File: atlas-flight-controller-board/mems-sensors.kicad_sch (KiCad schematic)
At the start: 11 parts

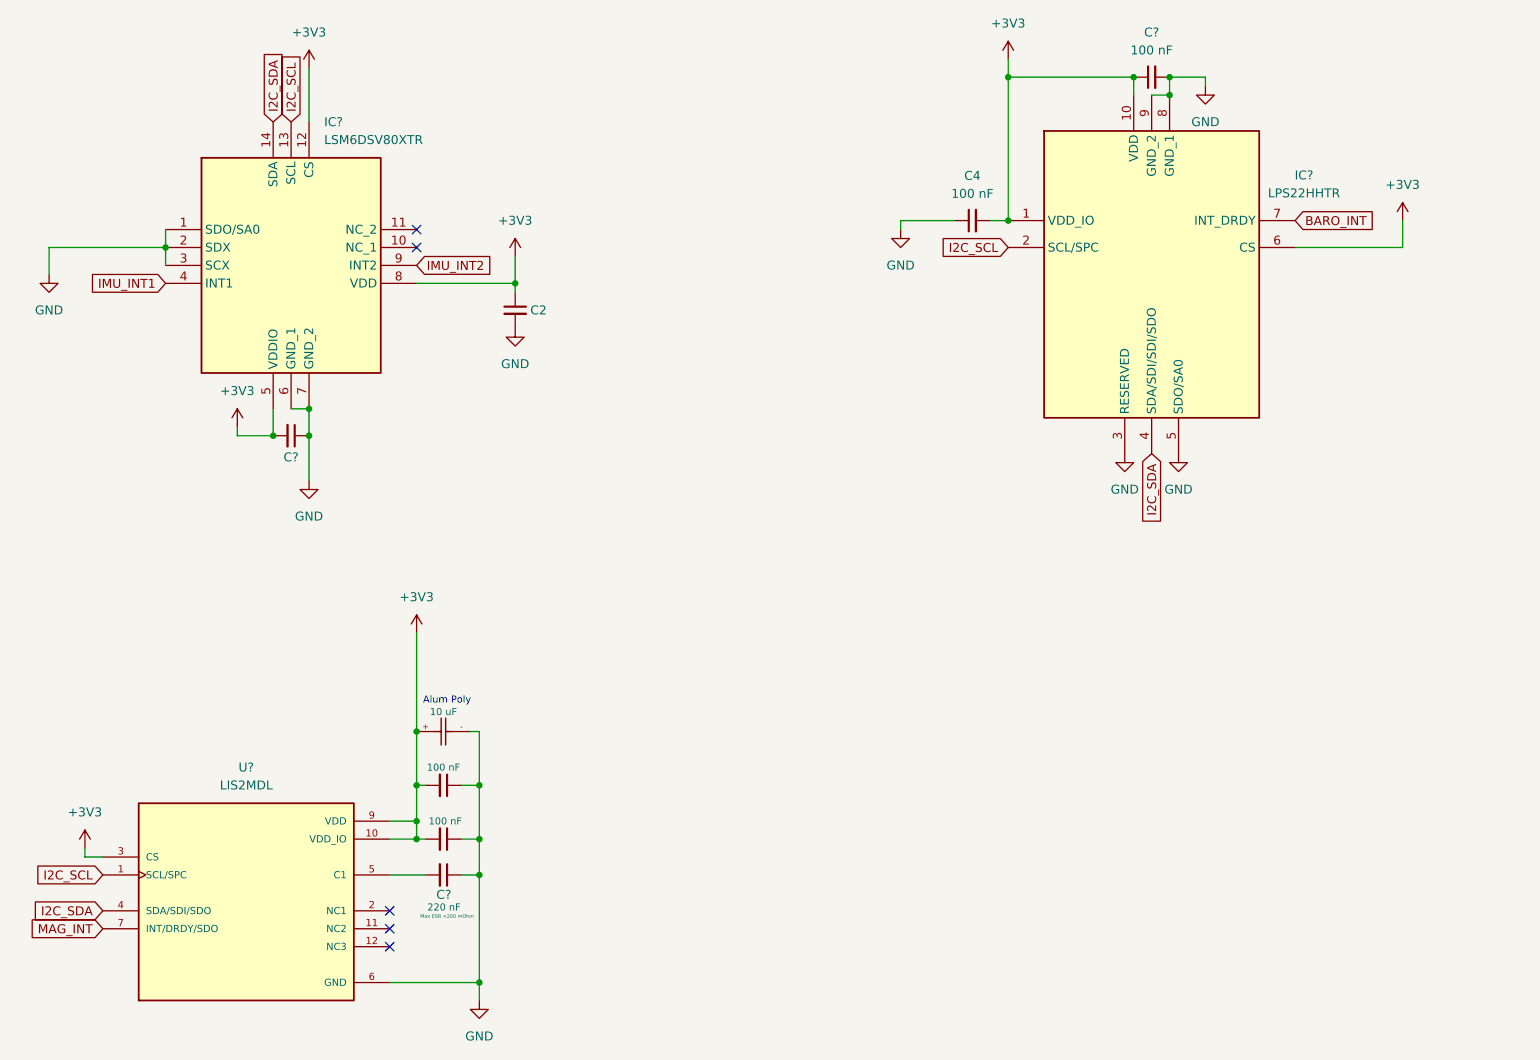
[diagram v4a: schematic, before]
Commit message: Added Regulator, Leaving disconnected, and off pcb for now as teensy board does this automatically. Leaving on for future revs without teensy board
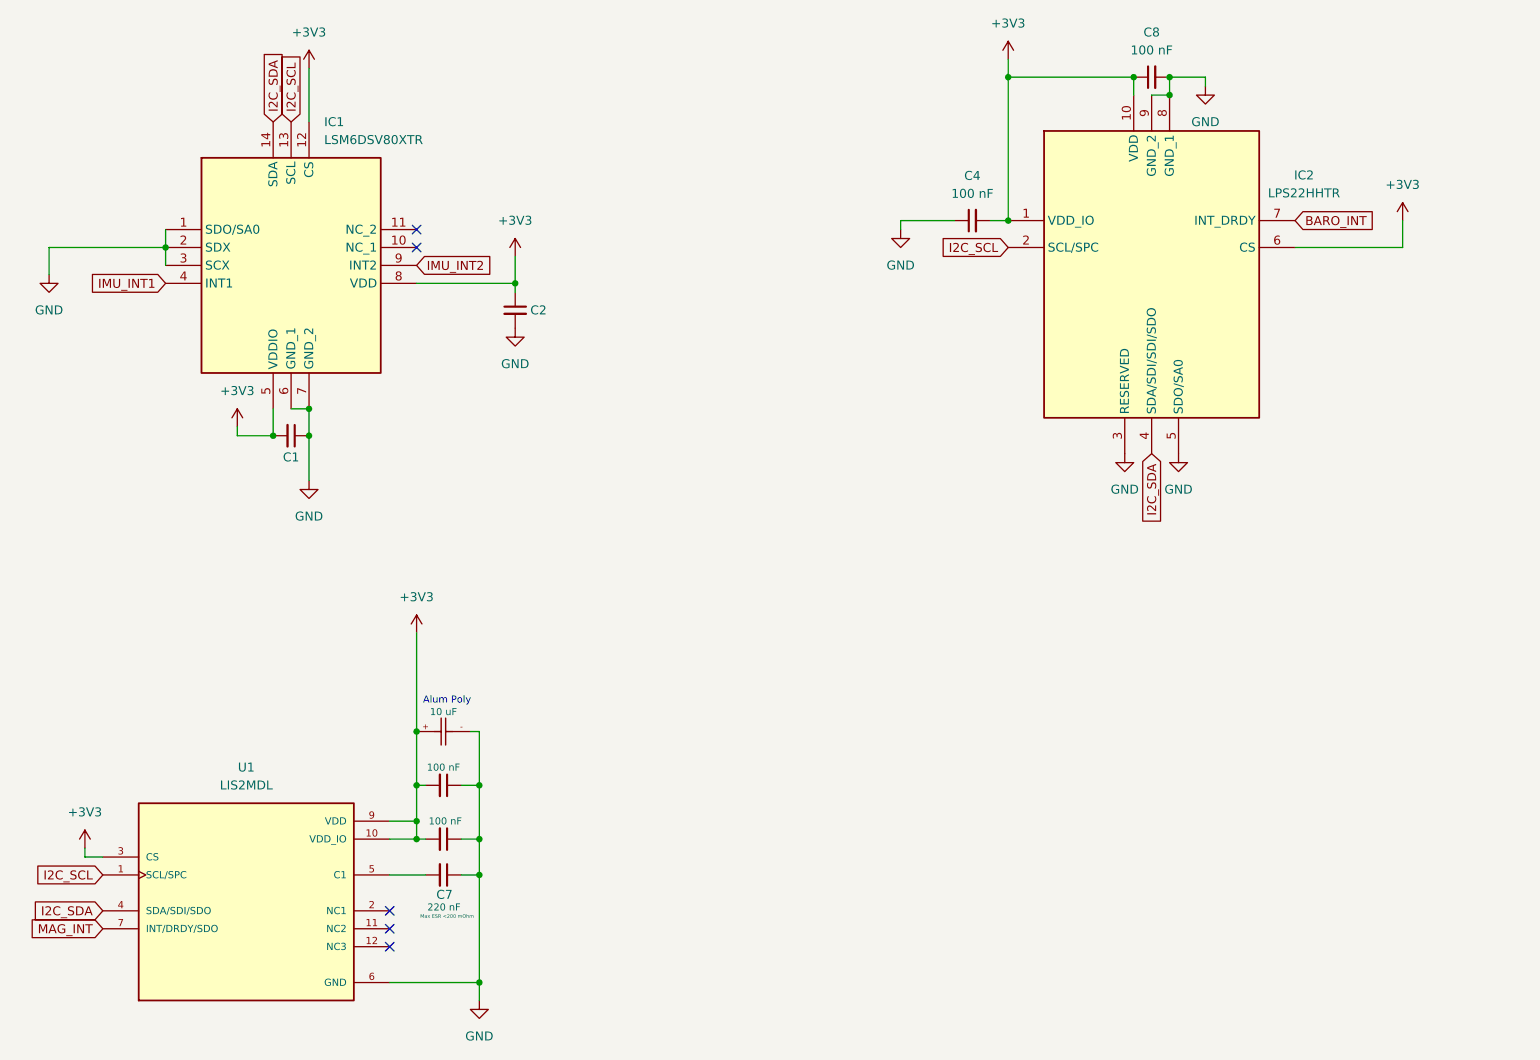
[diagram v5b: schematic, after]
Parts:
- gave numbers to parts that had none: 9
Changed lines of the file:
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@@
 		(on_board yes)
 		(dnp no)
-		(property "Reference" "C?"
+		(property "Reference" "C5"
 			(at 102.8636 134.62 90)
 			(effects
@@
 			(project "atlas-flight-controller-board"
 				(path "/99efb2d6-b5f7-438c-9ed2-f359400f01a1/5584e1ef-6e93-420a-9bdf-15a5926ce2b3"
-					(reference "C?")
+					(reference "C5")
 					(unit 1)
 				)
@@
 		(dnp no)
 		(fields_autoplaced yes)
-		(property "Reference" "#PWR?"
+		(property "Reference" "#PWR0109"
 			(at 46.99 74.93 0)
 			(effects
@@
 			(project "atlas-flight-controller-board"
 				(path "/99efb2d6-b5f7-438c-9ed2-f359400f01a1/5584e1ef-6e93-420a-9bdf-15a5926ce2b3"
-					(reference "#PWR?")
+					(reference "#PWR0109")
 					(unit 1)
 				)
@@
 		(dnp no)
 		(fields_autoplaced yes)
-		(property "Reference" "#PWR?"
+		(property "Reference" "#PWR0108"
 			(at 99.06 123.19 0)
 			(effects
@@
 			(project "atlas-flight-controller-board"
 				(path "/99efb2d6-b5f7-438c-9ed2-f359400f01a1/5584e1ef-6e93-420a-9bdf-15a5926ce2b3"
-					(reference "#PWR?")
+					(reference "#PWR0108")
 					(unit 1)
 				)
@@
 		(dnp no)
 		(fields_autoplaced yes)
-		(property "Reference" "#PWR?"
+		(property "Reference" "#PWR0113"
 			(at 113.03 69.85 0)
 			(effects
@@
 			(project "atlas-flight-controller-board"
 				(path "/99efb2d6-b5f7-438c-9ed2-f359400f01a1/5584e1ef-6e93-420a-9bdf-15a5926ce2b3"
-					(reference "#PWR?")
+					(reference "#PWR0113")
 					(unit 1)
 				)
@@
 		(dnp no)
 		(fields_autoplaced yes)
-		(property "Reference" "#PWR?"
+		(property "Reference" "#PWR0112"
 			(at 83.82 104.14 0)
 			(effects
@@
 			(project "atlas-flight-controller-board"
 				(path "/99efb2d6-b5f7-438c-9ed2-f359400f01a1/5584e1ef-6e93-420a-9bdf-15a5926ce2b3"
-					(reference "#PWR?")
+					(reference "#PWR0112")
 					(unit 1)
 				)
@@
 		(dnp no)
 		(fields_autoplaced yes)
-		(property "Reference" "#PWR?"
+		(property "Reference" "#PWR0103"
 			(at 210.82 48.26 0)
 			(effects
@@
 			(project "atlas-flight-controller-board"
 				(path "/99efb2d6-b5f7-438c-9ed2-f359400f01a1/5584e1ef-6e93-420a-9bdf-15a5926ce2b3"
-					(reference "#PWR?")
+					(reference "#PWR0103")
 					(unit 1)
 				)
@@
 		(dnp no)
 		(fields_autoplaced yes)
-		(property "Reference" "#PWR?"
+		(property "Reference" "#PWR0105"
 			(at 182.88 41.91 0)
 			(effects
@@
 			(project "atlas-flight-controller-board"
 				(path "/99efb2d6-b5f7-438c-9ed2-f359400f01a1/5584e1ef-6e93-420a-9bdf-15a5926ce2b3"
-					(reference "#PWR?")
+					(reference "#PWR0105")
 					(unit 1)
 				)
@@
 		(on_board yes)
 		(dnp no)
-		(property "Reference" "C?"
+		(property "Reference" "C6"
 			(at 102.616 144.272 90)
 			(effects
@@
 			(project "atlas-flight-controller-board"
 				(path "/99efb2d6-b5f7-438c-9ed2-f359400f01a1/5584e1ef-6e93-420a-9bdf-15a5926ce2b3"
-					(reference "C?")
+					(reference "C6")
 					(unit 1)
 				)
@@
 		(dnp no)
 		(fields_autoplaced yes)
-		(property "Reference" "IC?"
+		(property "Reference" "IC2"
 			(at 224.79 54.5398 0)
 			(effects
@@
 			(project "atlas-flight-controller-board"
 				(path "/99efb2d6-b5f7-438c-9ed2-f359400f01a1/5584e1ef-6e93-420a-9bdf-15a5926ce2b3"
-					(reference "IC?")
+					(reference "IC2")
 					(unit 1)
 				)
@@
 		(on_board yes)
 		(dnp no)
-		(property "Reference" "C?"
+		(property "Reference" "C3"
 			(at 102.87 127 0)
 			(effects
@@
 			(project "atlas-flight-controller-board"
 				(path "/99efb2d6-b5f7-438c-9ed2-f359400f01a1/5584e1ef-6e93-420a-9bdf-15a5926ce2b3"
-					(reference "C?")
+					(reference "C3")
 					(unit 1)
 				)
@@
 		(dnp no)
 		(fields_autoplaced yes)
-		(property "Reference" "C?"
+		(property "Reference" "C8"
 			(at 203.2063 34.29 90)
 			(effects
@@
 			(project "atlas-flight-controller-board"
 				(path "/99efb2d6-b5f7-438c-9ed2-f359400f01a1/5584e1ef-6e93-420a-9bdf-15a5926ce2b3"
-					(reference "C?")
+					(reference "C8")
 					(unit 1)
 				)
@@
 		(dnp no)
 		(fields_autoplaced yes)
-		(property "Reference" "#PWR?"
+		(property "Reference" "#PWR0110"
 			(at 73.66 93.98 0)
 			(effects
@@
 			(project "atlas-flight-controller-board"
 				(path "/99efb2d6-b5f7-438c-9ed2-f359400f01a1/5584e1ef-6e93-420a-9bdf-15a5926ce2b3"
-					(reference "#PWR?")
+					(reference "#PWR0110")
 					(unit 1)
 				)
@@
 		(dnp no)
 		(fields_autoplaced yes)
-		(property "Reference" "#PWR?"
+		(property "Reference" "#PWR0102"
 			(at 167.64 68.58 0)
 			(effects
@@
 			(project "atlas-flight-controller-board"
 				(path "/99efb2d6-b5f7-438c-9ed2-f359400f01a1/5584e1ef-6e93-420a-9bdf-15a5926ce2b3"
-					(reference "#PWR?")
+					(reference "#PWR0102")
 					(unit 1)
 				)
@@
 		(on_board yes)
 		(dnp no)
-		(property "Reference" "C?"
+		(property "Reference" "C1"
 			(at 81.28 94.488 90)
 			(effects
@@
 			(project "atlas-flight-controller-board"
 				(path "/99efb2d6-b5f7-438c-9ed2-f359400f01a1/5584e1ef-6e93-420a-9bdf-15a5926ce2b3"
-					(reference "C?")
+					(reference "C1")
 					(unit 1)
 				)
@@
 		(dnp no)
 		(fields_autoplaced yes)
-		(property "Reference" "#PWR?"
+		(property "Reference" "#PWR0101"
 			(at 107.95 177.8 0)
 			(effects
@@
 			(project "atlas-flight-controller-board"
 				(path "/99efb2d6-b5f7-438c-9ed2-f359400f01a1/5584e1ef-6e93-420a-9bdf-15a5926ce2b3"
-					(reference "#PWR?")
+					(reference "#PWR0101")
 					(unit 1)
 				)
@@
 		(dnp no)
 		(fields_autoplaced yes)
-		(property "Reference" "U?"
+		(property "Reference" "U1"
 			(at 74.93 138.43 0)
 			(effects
@@
 			(project "atlas-flight-controller-board"
 				(path "/99efb2d6-b5f7-438c-9ed2-f359400f01a1/5584e1ef-6e93-420a-9bdf-15a5926ce2b3"
-					(reference "U?")
+					(reference "U1")
 					(unit 1)
 				)
@@
 		(dnp no)
 		(fields_autoplaced yes)
-		(property "Reference" "#PWR?"
+		(property "Reference" "#PWR0111"
 			(at 52.07 153.67 0)
 			(effects
@@
 			(project "atlas-flight-controller-board"
 				(path "/99efb2d6-b5f7-438c-9ed2-f359400f01a1/5584e1ef-6e93-420a-9bdf-15a5926ce2b3"
-					(reference "#PWR?")
+					(reference "#PWR0111")
 					(unit 1)
 				)
@@
 		(dnp no)
 		(fields_autoplaced yes)
-		(property "Reference" "#PWR?"
+		(property "Reference" "#PWR0114"
 			(at 83.82 43.18 0)
 			(effects
@@
 			(project "atlas-flight-controller-board"
 				(path "/99efb2d6-b5f7-438c-9ed2-f359400f01a1/5584e1ef-6e93-420a-9bdf-15a5926ce2b3"
-					(reference "#PWR?")
+					(reference "#PWR0114")
 					(unit 1)
 				)
@@
 		(dnp no)
 		(fields_autoplaced yes)
-		(property "Reference" "#PWR?"
+		(property "Reference" "#PWR0106"
 			(at 207.01 100.33 0)
 			(effects
@@
 			(project "atlas-flight-controller-board"
 				(path "/99efb2d6-b5f7-438c-9ed2-f359400f01a1/5584e1ef-6e93-420a-9bdf-15a5926ce2b3"
-					(reference "#PWR?")
+					(reference "#PWR0106")
 					(unit 1)
 				)
@@
 		(on_board yes)
 		(dnp no)
-		(property "Reference" "C?"
+		(property "Reference" "C7"
 			(at 101.854 156.464 90)
 			(effects
@@
 			(project "atlas-flight-controller-board"
 				(path "/99efb2d6-b5f7-438c-9ed2-f359400f01a1/5584e1ef-6e93-420a-9bdf-15a5926ce2b3"
-					(reference "C?")
+					(reference "C7")
 					(unit 1)
 				)
@@
 		(dnp no)
 		(fields_autoplaced yes)
-		(property "Reference" "#PWR?"
+		(property "Reference" "#PWR0104"
 			(at 238.76 64.77 0)
 			(effects
@@
 			(project "atlas-flight-controller-board"
 				(path "/99efb2d6-b5f7-438c-9ed2-f359400f01a1/5584e1ef-6e93-420a-9bdf-15a5926ce2b3"
-					(reference "#PWR?")
+					(reference "#PWR0104")
 					(unit 1)
 				)
@@
 		(dnp no)
 		(fields_autoplaced yes)
-		(property "Reference" "#PWR?"
+		(property "Reference" "#PWR0107"
 			(at 199.39 100.33 0)
 			(effects
@@
 			(project "atlas-flight-controller-board"
 				(path "/99efb2d6-b5f7-438c-9ed2-f359400f01a1/5584e1ef-6e93-420a-9bdf-15a5926ce2b3"
-					(reference "#PWR?")
+					(reference "#PWR0107")
 					(unit 1)
 				)
@@
 		(dnp no)
 		(fields_autoplaced yes)
-		(property "Reference" "IC?"
+		(property "Reference" "IC1"
 			(at 85.9633 46.99 0)
 			(effects
@@
 			(project "atlas-flight-controller-board"
 				(path "/99efb2d6-b5f7-438c-9ed2-f359400f01a1/5584e1ef-6e93-420a-9bdf-15a5926ce2b3"
-					(reference "IC?")
+					(reference "IC1")
 					(unit 1)
 				)
@@
 		(dnp no)
 		(fields_autoplaced yes)
-		(property "Reference" "#PWR?"
+		(property "Reference" "#PWR0115"
 			(at 113.03 82.55 0)
 			(effects
@@
 			(project "atlas-flight-controller-board"
 				(path "/99efb2d6-b5f7-438c-9ed2-f359400f01a1/5584e1ef-6e93-420a-9bdf-15a5926ce2b3"
-					(reference "#PWR?")
-					(unit 1)
-				)
+					(reference "#PWR0115")
+					(unit 1)
+				)

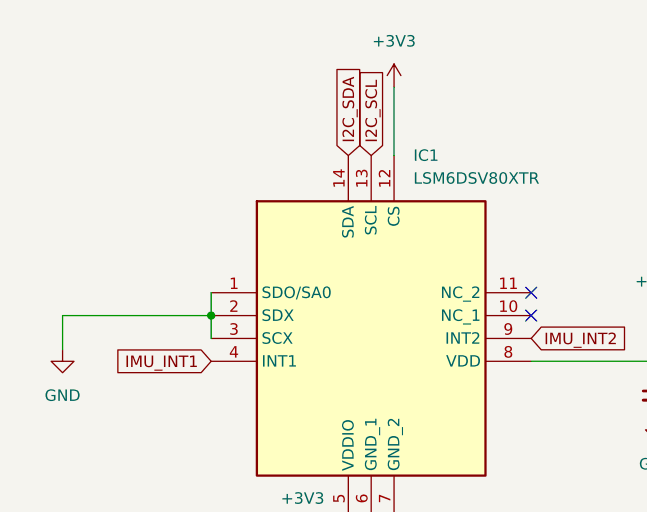
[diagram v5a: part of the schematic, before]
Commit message: Updating IMU to SPI
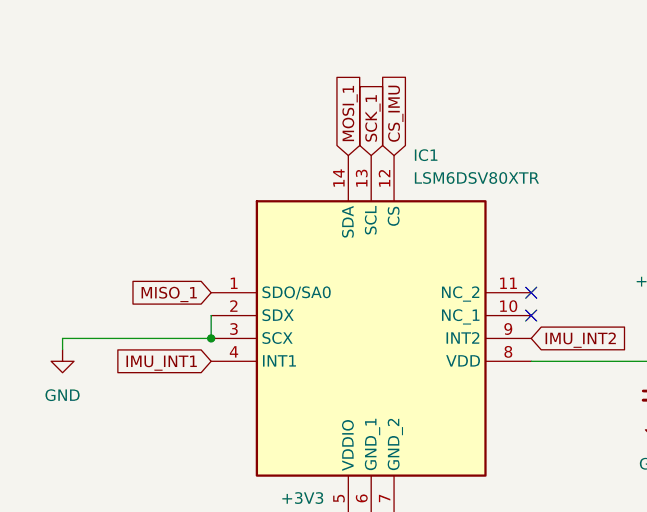
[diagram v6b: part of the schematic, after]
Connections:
- net +3V3: no longer IC1.12 (CS)
- net GND: no longer IC1.1 (SDO/SA0)
- net I2C_SCL: no longer IC1.13 (SCL)
- net I2C_SDA: no longer IC1.14 (SDA)
- new net CS_IMU: IC1.12 (CS)
- new net MISO_1: IC1.1 (SDO/SA0)
- new net MOSI_1: IC1.14 (SDA)
- new net SCK_1: IC1.13 (SCL)
